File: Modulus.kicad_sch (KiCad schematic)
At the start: 208 parts, among them J1 USB_C_Receptacle_USB2.0_14P, SW1 Push_Button, U1 RP2040, U2 NCP1117-1.5_SOT223, U3 W25Q128JVS, Y1 12MHz

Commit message: added LEDs, may remove
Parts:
- added C100, C101, C102, C103, C104, C105, C106, C18, C19, C20, C21, C22, C23, C24, C25, C26, C27, C28, C29, C30, C31, C32, C33, C34, C35, C36, C37, C38, C39, C40, C41, C42, C43, C44, C45, C46, C47, C48, C49, C50, C51, C52, C53, C54, C55, C56, C57, C58, C59, C60, C61, C62, C63, C64, C65, C66, C67, C68, C69, C70, C71, C72, C73, C74, C75, C76, C77, C78, C79, C80, C81, C82, C83, C84, C85, C86, C87, C88, C89, C90, C91, C92, C93, C94, C95, C96, C97, C98, C99: 100nF, Capacitor_SMD:C_0402_1005Metric, symbol Device:C
- added D100, D101, D102, D103, D104, D105, D106, D107, D108, D109, D110, D111, D112, D113, D114, D115, D116, D117, D118, D119, D120, D121, D122, D123, D124, D125, D126, D127, D128, D129, D130, D131, D132, D133, D134, D135, D136, D137, D138, D139, D140, D141, D142, D143, D144, D145, D146, D147, D148, D149, D150, D151, D152, D153, D154, D155, D156, D157, D158, D159, D160, D161, D162, D163, D164, D165, D166, D167, D168, D169, D170, D171, D172, D173, D174, D175, D176, D177, D178, D179, D180, D181, D182, D183, D184, D90, D91, D92, D93, D94, D95, D96, D97, D98, D99: SK6812MINI, LED_SMD:LED_SK6812MINI_PLCC4_3.5x3.5mm_P1.75mm, symbol LED:SK6812MINI
- C15, C16: value 15pF -> 33pF
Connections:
- net +3V3: now also C100.2, C101.2, C102.2, C103.2, C104.2, C105.2, C106.2, C18.2, C19.2, C20.2, C21.2, C22.2, C23.2, C24.2, C25.2, C26.2, C27.2, C28.2, C29.2, C30.2, C31.2, C32.2, C33.2, C34.2, C35.2, C36.2, C37.2, C38.2, C39.2, C40.2, C41.2, C42.2, C43.2, C44.2, C45.2, C46.2, C47.2, C48.2, C49.2, C50.2, C51.2, C52.2, C53.2, C54.2, C55.2, C56.2, C57.2, C58.2, C59.2, C60.2, C61.2, C62.2, C63.2, C64.2, C65.2, C66.2, C67.2, C68.2, C69.2, C70.2, C71.2, C72.2, C73.2, C74.2, C75.2, C76.2, C77.2, C78.2, C79.2, C80.2, C81.2, C82.2, C83.2, C84.2, C85.2, C86.2, C87.2, C88.2, C89.2, C90.2, C91.2, C92.2, C93.2, C94.2, C95.2, C96.2, C97.2, C98.2, C99.2, D100.4 (VDD), D101.4 (VDD), D102.4 (VDD), D103.4 (VDD), D104.4 (VDD), D105.4 (VDD), D106.4 (VDD), D107.4 (VDD), D108.4 (VDD), D109.4 (VDD), D110.4 (VDD), D111.4 (VDD), D112.4 (VDD), D113.4 (VDD), D114.4 (VDD), D115.4 (VDD), D116.4 (VDD), D117.4 (VDD), D118.4 (VDD), D119.4 (VDD), D120.4 (VDD), D121.4 (VDD), D90.4 (VDD), D91.4 (VDD), D92.4 (VDD), D93.4 (VDD), D94.4 (VDD), D95.4 (VDD), D96.4 (VDD), D97.4 (VDD), D98.4 (VDD), D99.4 (VDD)
- net GND: now also C100.1, C101.1, C102.1, C103.1, C104.1, C105.1, C106.1, C18.1, C19.1, C20.1, C21.1, C22.1, C23.1, C24.1, C25.1, C26.1, C27.1, C28.1, C29.1, C30.1, C31.1, C32.1, C33.1, C34.1, C35.1, C36.1, C37.1, C38.1, C39.1, C40.1, C41.1, C42.1, C43.1, C44.1, C45.1, C46.1, C47.1, C48.1, C49.1, C50.1, C51.1, C52.1, C53.1, C54.1, C55.1, C56.1, C57.1, C58.1, C59.1, C60.1, C61.1, C62.1, C63.1, C64.1, C65.1, C66.1, C67.1, C68.1, C69.1, C70.1, C71.1, C72.1, C73.1, C74.1, C75.1, C76.1, C77.1, C78.1, C79.1, C80.1, C81.1, C82.1, C83.1, C84.1, C85.1, C86.1, C87.1, C88.1, C89.1, C90.1, C91.1, C92.1, C93.1, C94.1, C95.1, C96.1, C97.1, C98.1, C99.1, D100.2 (VSS), D101.2 (VSS), D102.2 (VSS), D103.2 (VSS), D104.2 (VSS), D105.2 (VSS), D106.2 (VSS), D107.2 (VSS), D108.2 (VSS), D109.2 (VSS), D110.2 (VSS), D111.2 (VSS), D112.2 (VSS), D113.2 (VSS), D114.2 (VSS), D115.2 (VSS), D116.2 (VSS), D117.2 (VSS), D118.2 (VSS), D119.2 (VSS), D120.2 (VSS), D121.2 (VSS), D137.2 (VSS), D138.2 (VSS), D139.2 (VSS), D140.2 (VSS), D141.2 (VSS), D142.2 (VSS), D143.2 (VSS), D144.2 (VSS), D145.2 (VSS), D146.2 (VSS), D147.2 (VSS), D148.2 (VSS), D149.2 (VSS), D150.2 (VSS), D151.2 (VSS), D152.2 (VSS), D153.2 (VSS), D154.2 (VSS), D155.2 (VSS), D156.2 (VSS), D157.2 (VSS), D158.2 (VSS), D159.2 (VSS), D160.2 (VSS), D161.2 (VSS), D162.2 (VSS), D163.2 (VSS), D164.2 (VSS), D165.2 (VSS), D166.2 (VSS), D167.2 (VSS), D168.2 (VSS), D169.2 (VSS), D170.2 (VSS), D171.2 (VSS), D172.2 (VSS), D173.2 (VSS), D174.2 (VSS), D175.2 (VSS), D176.2 (VSS), D177.2 (VSS), D178.2 (VSS), D179.2 (VSS), D180.2 (VSS), D181.2 (VSS), D182.2 (VSS), D183.2 (VSS), D184.2 (VSS), D90.2 (VSS), D91.2 (VSS), D92.2 (VSS), D93.2 (VSS), D94.2 (VSS), D95.2 (VSS), D96.2 (VSS), D97.2 (VSS), D98.2 (VSS), D99.2 (VSS)
- new net: D179.1 (DOUT), D180.3 (DIN)
- new net: D178.1 (DOUT), D179.3 (DIN)
- new net: D152.4 (VDD), D153.4 (VDD), D154.4 (VDD), D155.4 (VDD), D156.4 (VDD), D157.4 (VDD), D158.4 (VDD), D159.4 (VDD), D160.4 (VDD), D161.4 (VDD), D162.4 (VDD), D163.4 (VDD), D164.4 (VDD), D165.4 (VDD), D166.4 (VDD), D167.4 (VDD), D168.4 (VDD), D169.4 (VDD), D170.4 (VDD), D171.4 (VDD), D172.4 (VDD), D173.4 (VDD), D174.4 (VDD), D175.4 (VDD), D176.4 (VDD), D177.4 (VDD), D178.4 (VDD), D179.4 (VDD), D180.4 (VDD), D181.4 (VDD), D182.4 (VDD), D183.4 (VDD), D184.4 (VDD)
- new net: D144.1 (DOUT), D145.3 (DIN)
- new net: D143.1 (DOUT), D144.3 (DIN)
- new net: D122.4 (VDD), D123.4 (VDD), D124.4 (VDD), D125.4 (VDD), D126.4 (VDD), D127.4 (VDD), D128.4 (VDD), D129.4 (VDD), D130.4 (VDD), D131.4 (VDD), D132.4 (VDD), D133.4 (VDD), D134.4 (VDD), D135.4 (VDD), D136.4 (VDD), D137.4 (VDD), D138.4 (VDD), D139.4 (VDD), D140.4 (VDD), D141.4 (VDD), D142.4 (VDD), D143.4 (VDD), D144.4 (VDD), D145.4 (VDD), D146.4 (VDD), D147.4 (VDD), D148.4 (VDD), D149.4 (VDD), D150.4 (VDD), D151.4 (VDD)
- new net: D175.1 (DOUT), D176.3 (DIN)
- new net: D174.1 (DOUT), D175.3 (DIN)
- new net: D150.1 (DOUT), D151.3 (DIN)
- new net: D149.1 (DOUT), D150.3 (DIN)
- new net: D151.1 (DOUT), D152.3 (DIN)
- new net: D167.1 (DOUT), D168.3 (DIN)
- new net: D166.1 (DOUT), D167.3 (DIN)
- new net: D142.1 (DOUT), D143.3 (DIN)
- new net: D96.1 (DOUT), D97.3 (DIN)
- new net: D95.1 (DOUT), D96.3 (DIN)
- new net: D140.1 (DOUT), D141.3 (DIN)
- new net: D139.1 (DOUT), D140.3 (DIN)
- new net: D128.1 (DOUT), D129.3 (DIN)
- new net: D127.1 (DOUT), D128.3 (DIN)
- new net: D181.1 (DOUT), D182.3 (DIN)
- new net: D180.1 (DOUT), D181.3 (DIN)
- new net: D141.1 (DOUT), D142.3 (DIN)
- new net: D173.1 (DOUT), D174.3 (DIN)
- new net: D145.1 (DOUT), D146.3 (DIN)
- new net: D117.1 (DOUT), D118.3 (DIN)
- new net: D116.1 (DOUT), D117.3 (DIN)
- new net: D129.1 (DOUT), D130.3 (DIN)
- new net: D155.1 (DOUT), D156.3 (DIN)
- new net: D154.1 (DOUT), D155.3 (DIN)
- new net: D94.1 (DOUT), D95.3 (DIN)
- new net: D93.1 (DOUT), D94.3 (DIN)
- new net: D101.1 (DOUT), D102.3 (DIN)
- new net: D100.1 (DOUT), D101.3 (DIN)
- new net: D130.1 (DOUT), D131.3 (DIN)
- new net: D169.1 (DOUT), D170.3 (DIN)
- new net: D168.1 (DOUT), D169.3 (DIN)
- new net: D114.1 (DOUT), D115.3 (DIN)
- new net: D113.1 (DOUT), D114.3 (DIN)
- new net: D100.3 (DIN), D99.1 (DOUT)
- new net: D148.1 (DOUT), D149.3 (DIN)
- new net: D147.1 (DOUT), D148.3 (DIN)
- new net: D171.1 (DOUT), D172.3 (DIN)
- new net: D170.1 (DOUT), D171.3 (DIN)
- new net: D157.1 (DOUT), D158.3 (DIN)
- new net: D156.1 (DOUT), D157.3 (DIN)
- new net: D164.1 (DOUT), D165.3 (DIN)
- new net: D163.1 (DOUT), D164.3 (DIN)
- new net: D159.1 (DOUT), D160.3 (DIN)
- new net: D158.1 (DOUT), D159.3 (DIN)
- new net: D125.1 (DOUT), D126.3 (DIN)
- new net: D124.1 (DOUT), D125.3 (DIN)
- new net: D112.1 (DOUT), D113.3 (DIN)
- new net: D111.1 (DOUT), D112.3 (DIN)
- new net: D183.1 (DOUT), D184.3 (DIN)
- new net: D182.1 (DOUT), D183.3 (DIN)
- new net: D115.1 (DOUT), D116.3 (DIN)
- new net: D146.1 (DOUT), D147.3 (DIN)
- new net: D160.1 (DOUT), D161.3 (DIN)
- new net: D92.1 (DOUT), D93.3 (DIN)
- new net: D91.1 (DOUT), D92.3 (DIN)
- new net: D110.1 (DOUT), D111.3 (DIN)
- new net: D131.1 (DOUT), D132.3 (DIN)
- new net: D121.1 (DOUT), D122.3 (DIN)
- new net: D120.1 (DOUT), D121.3 (DIN)
- new net: D90.1 (DOUT), D91.3 (DIN)
- new net: D177.1 (DOUT), D178.3 (DIN)
- new net: D153.1 (DOUT), D154.3 (DIN)
- new net: D119.1 (DOUT), D120.3 (DIN)
- new net: D118.1 (DOUT), D119.3 (DIN)
- new net: D104.1 (DOUT), D105.3 (DIN)
- new net: D103.1 (DOUT), D104.3 (DIN)
- new net: D152.1 (DOUT), D153.3 (DIN)
- new net: D106.1 (DOUT), D107.3 (DIN)
- new net: D105.1 (DOUT), D106.3 (DIN)
- new net: D162.1 (DOUT), D163.3 (DIN)
- new net: D176.1 (DOUT), D177.3 (DIN)
- new net: D137.1 (DOUT), D138.3 (DIN)
- new net: D136.1 (DOUT), D137.3 (DIN)
- new net: D102.1 (DOUT), D103.3 (DIN)
- new net: D138.1 (DOUT), D139.3 (DIN)
- new net: D109.1 (DOUT), D110.3 (DIN)
- new net: D108.1 (DOUT), D109.3 (DIN)
- new net: D165.1 (DOUT), D166.3 (DIN)
- new net: D172.1 (DOUT), D173.3 (DIN)
- new net: D135.1 (DOUT), D136.3 (DIN)
- new net: D134.1 (DOUT), D135.3 (DIN)
- new net: D132.1 (DOUT), D133.3 (DIN)
- new net: D107.1 (DOUT), D108.3 (DIN)
- new net: D123.1 (DOUT), D124.3 (DIN)
- new net: D122.1 (DOUT), D123.3 (DIN)
- new net: D98.1 (DOUT), D99.3 (DIN)
- new net: D97.1 (DOUT), D98.3 (DIN)
- new net: D161.1 (DOUT), D162.3 (DIN)
- new net: D133.1 (DOUT), D134.3 (DIN)
- new net: D126.1 (DOUT), D127.3 (DIN)
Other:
- note added: "LED Matrix"
- note added: "Matrix Smoothing"
- company: (none) -> contykeys
- title: (none) -> Modules - Mainboard

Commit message: added a USB hub but don't really understand shit rn
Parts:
- removed C100, C101, C102, C103, C104, C105, C106, C18, C19, C20, C21, C22, C23, C24, C25, C26, C27, C28, C29, C30, C31, C32, C33, C34, C35, C36, C37, C38, C39, C40, C41, C42, C43, C44, C45, C46, C47, C48, C49, C50, C51, C52, C53, C54, C55, C56, C57, C58, C59, C60, C61, C62, C63, C64, C65, C66, C67, C68, C69, C70, C71, C72, C73, C74, C75, C76, C77, C78, C79, C80, C81, C82, C83, C84, C85, C86, C87, C88, C89, C90, C91, C92, C93, C94, C95, C96, C97, C98, C99: 100nF, Capacitor_SMD:C_0402_1005Metric, symbol Device:C
- removed D100, D101, D102, D103, D104, D105, D106, D107, D108, D109, D110, D111, D112, D113, D114, D115, D116, D117, D118, D119, D120, D121, D122, D123, D124, D125, D126, D127, D128, D129, D130, D131, D132, D133, D134, D135, D136, D137, D138, D139, D140, D141, D142, D143, D144, D145, D146, D147, D148, D149, D150, D151, D152, D153, D154, D155, D156, D157, D158, D159, D160, D161, D162, D163, D164, D165, D166, D167, D168, D169, D170, D171, D172, D173, D174, D175, D176, D177, D178, D179, D180, D181, D182, D183, D184, D90, D91, D92, D93, D94, D95, D96, D97, D98, D99: SK6812MINI, LED_SMD:LED_SK6812MINI_PLCC4_3.5x3.5mm_P1.75mm, symbol LED:SK6812MINI
- removed J1: USB_C_Receptacle_USB2.0_14P, symbol Connector:USB_C_Receptacle_USB2.0_14P
- removed R2: 5.1K, Resistor_THT:R_Axial_DIN0207_L6.3mm_D2.5mm_P10.16mm_Horizontal, symbol PCM_SL_Resistors:Resistor
- added GL850G1: GL850G, GL850G:28SSOP, symbol GL850G:GL850G
- added J2: USB_C_Receptacle_USB2.0_14P, symbol Connector:USB_C_Receptacle_USB2.0_14P
- added J3, J4: USB_A, symbol Connector:USB_A
- added R8, R9: 5.1K, Resistor_THT:R_Axial_DIN0207_L6.3mm_D2.5mm_P10.16mm_Horizontal, symbol PCM_SL_Resistors:Resistor
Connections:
- net +3V3: now also GL850G1.24 (3V3)
- net GND: now also GL850G1.15 (GND), J2.A1 (GND), J2.A12 (GND), J2.B1 (GND), J2.B12 (GND), J2.S1 (SHIELD), J3.4 (GND), J3.5 (Shield), J4.4 (GND), J4.5 (Shield), R8.2, R9.2
- net VBUS: now also GL850G1.23 (5V), J2.A4 (VBUS), J2.A9 (VBUS), J2.B4 (VBUS), J2.B9 (VBUS), J3.1 (VBUS), J4.1 (VBUS)
- net at R1.1: now also GL850G1.4 (RREF)
- new net: J2.A5 (CC1), R8.1
- new net: J2.B5 (CC2), R9.1
- new net HOST_USB_D+: GL850G1.26 (DP0), J2.A6 (D+), J2.B6 (D+)
- new net HOST_USB_D-: GL850G1.25 (DM0), J2.A7 (D-), J2.B7 (D-)
- new net PORT1_USB_D+: GL850G1.28 (DP1), J3.3 (D+)
- new net PORT1_USB_D-: GL850G1.27 (DM1), J3.2 (D-)
- new net PORT2_USB_D+: GL850G1.3 (DP2), J4.3 (D+)
- new net PORT2_USB_D-: GL850G1.2 (DM2), J4.2 (D-)
- new net RP2040_USB_D+: GL850G1.9 (DP3)
- new net RP2040_USB_D-: GL850G1.8 (DM3)
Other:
- note removed: "LED Matrix"
- note removed: "Matrix Smoothing"
- moved on the sheet: C1, C10, C11, C12, C13, C14, C15, C16, C2, C3, C4, C5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

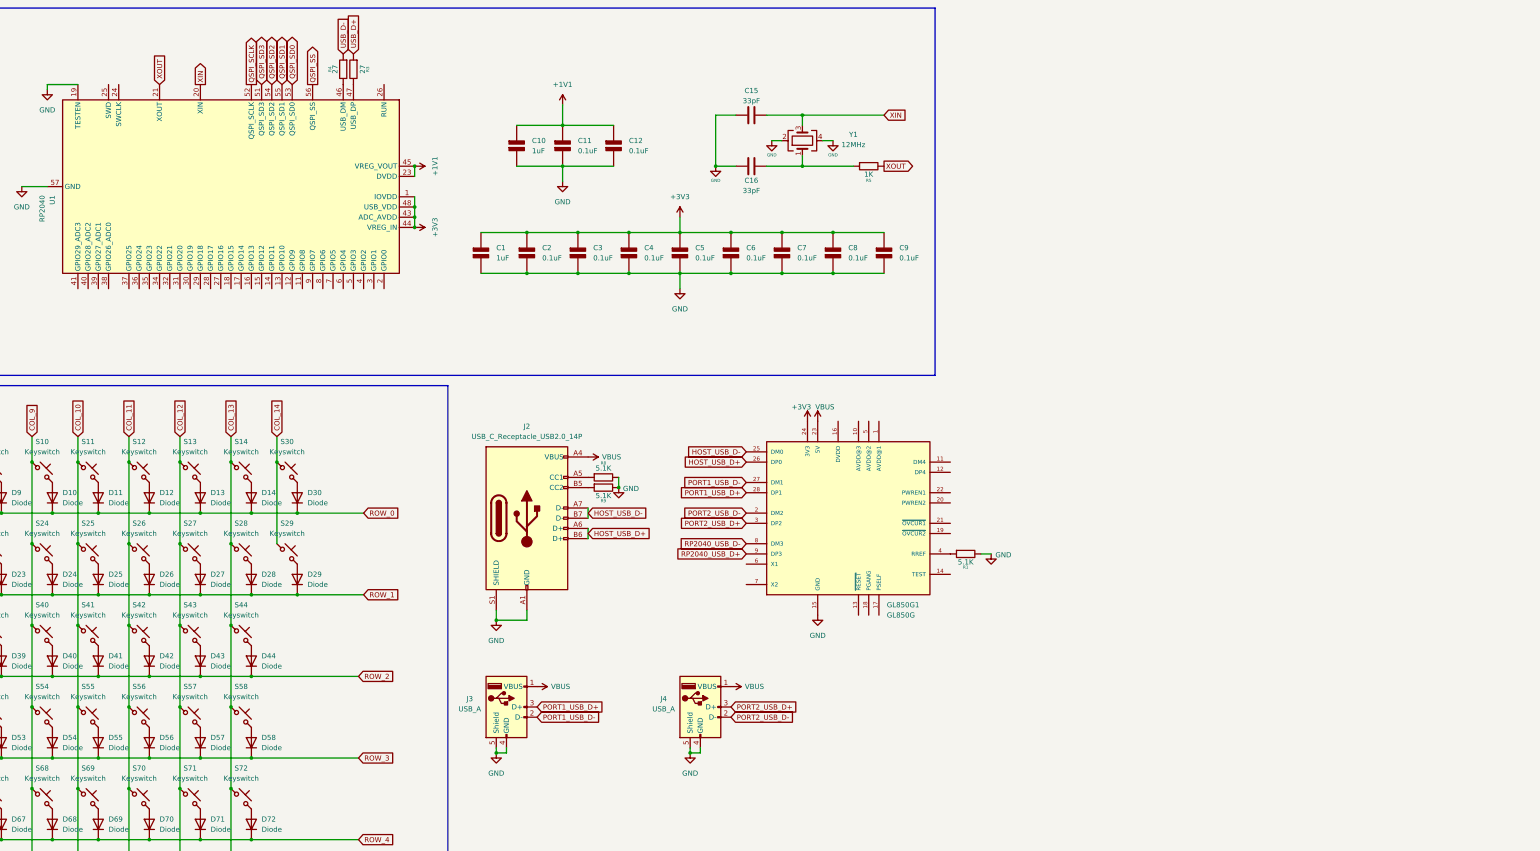
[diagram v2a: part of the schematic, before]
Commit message: added my own OLED screen, XLR ports, and a caps lock LEd
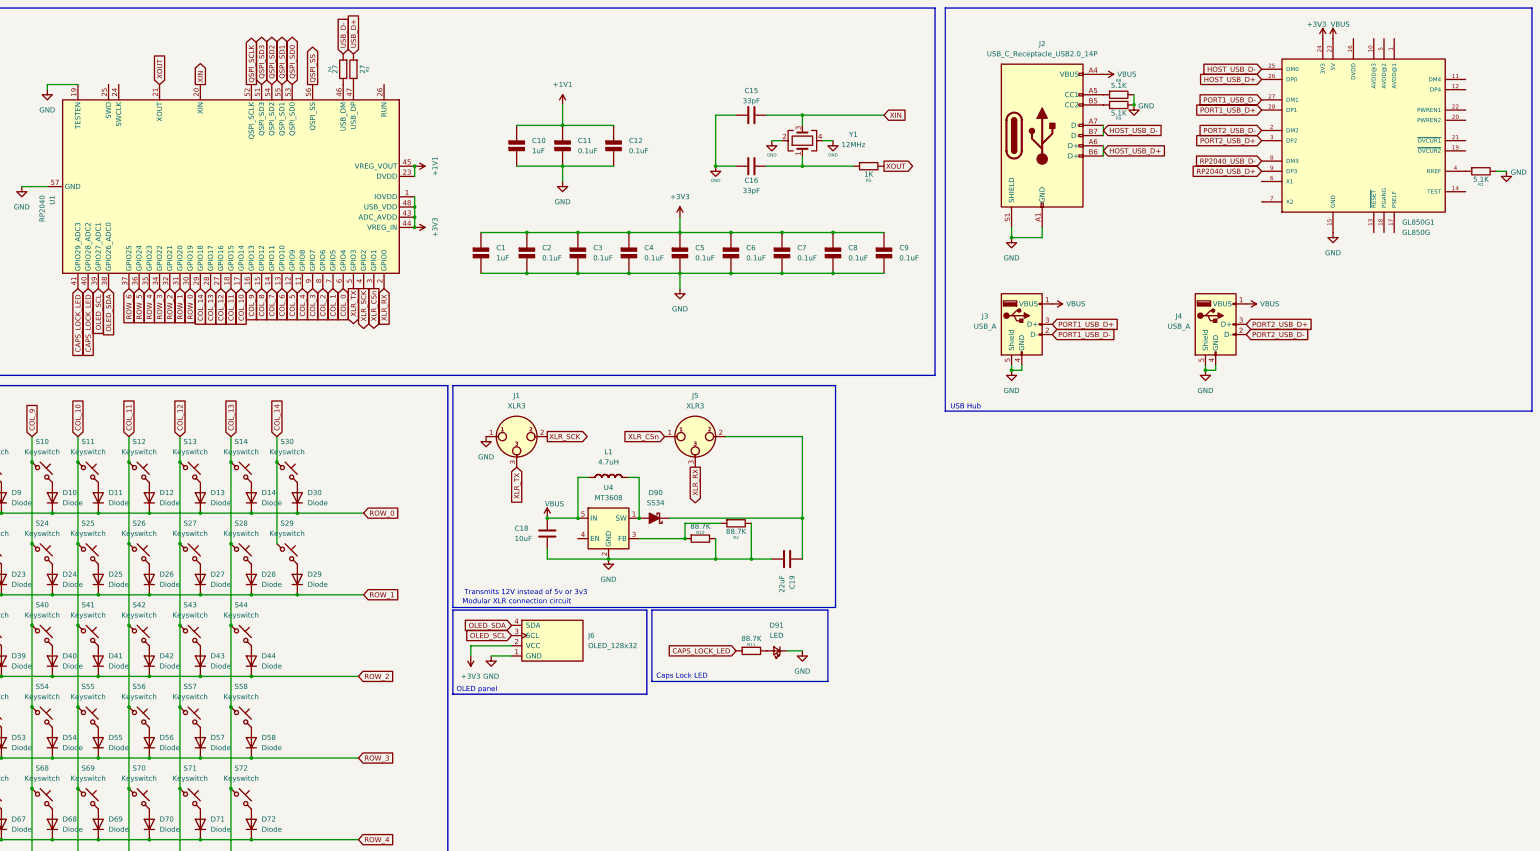
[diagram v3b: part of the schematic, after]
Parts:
- added C18: 10uF, symbol Device:C
- added C19: 22uF, symbol Device:C
- added D90: SS34, PCM_Diode_SMD_AKL:D_SMC, symbol PCM_Diode_Schottky_AKL:SS34
- added D91: LED, SparkFun-LED:LED_0603_1608Metric, symbol SparkFun-LED:LED
- added J1, J5: XLR3, symbol Connector_Audio:XLR3
- added J6: OLED_128x32, ScottoKeebs_Components:OLED_128x32, symbol SCOTOKEEBS:OLED_128x32
- added L1: 4.7uH, symbol PCM_Elektuur:L
- added R10, R11, R2: 88.7K, Resistor_THT:R_Axial_DIN0207_L6.3mm_D2.5mm_P10.16mm_Horizontal, symbol PCM_SL_Resistors:Resistor
- added U4: MT3608, Package_TO_SOT_SMD:SOT-23-6, symbol Regulator_Switching:MT3608
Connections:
- net +3V3: now also J6.2 (VCC)
- net COL_0: now also U1.6 (GPIO4)
- net COL_1: now also U1.7 (GPIO5)
- net COL_10: now also U1.17 (GPIO14)
- net COL_11: now also U1.18 (GPIO15)
- net COL_12: now also U1.27 (GPIO16)
- net COL_13: now also U1.28 (GPIO17)
- net COL_14: now also U1.29 (GPIO18)
- net COL_2: now also U1.8 (GPIO6)
- net COL_3: now also U1.9 (GPIO7)
- net COL_4: now also U1.11 (GPIO8)
- net COL_5: now also U1.12 (GPIO9)
- net COL_6: now also U1.13 (GPIO10)
- net COL_7: now also U1.14 (GPIO11)
- net COL_8: now also U1.15 (GPIO12)
- net COL_9: now also U1.16 (GPIO13)
- net GND: now also C18.2, C19.2, D91.1 (K), J1.1, J6.1 (GND), R10.2, R2.2, U4.2 (GND)
- net ROW_0: now also U1.30 (GPIO19)
- net ROW_1: now also U1.31 (GPIO20)
- net ROW_2: now also U1.32 (GPIO21)
- net ROW_3: now also U1.34 (GPIO22)
- net ROW_4: now also U1.35 (GPIO23)
- net ROW_5: now also U1.36 (GPIO24)
- net ROW_6: now also U1.37 (GPIO25)
- net VBUS: now also C18.1, L1.1 (+), U4.5 (IN)
- net XLR_RX: now reaches U1.2 (GPIO0)
- net XLR_RX: now also J5.3
- net XLR_CSn: now reaches U1.3 (GPIO1)
- net XLR_CSn: now also J5.1
- net OLED_SDA: now reaches U1.38 (GPIO26_ADC0)
- net OLED_SDA: now also J6.4 (SDA)
- net OLED_SCL: now reaches U1.39 (GPIO27_ADC1)
- net OLED_SCL: now also J6.3 (SCL)
- net XLR_SCK: now reaches U1.4 (GPIO2)
- net XLR_SCK: now also J1.2
- net CAPS_LOCK_LED: now reaches U1.40 (GPIO28_ADC2)
- net CAPS_LOCK_LED: now also U1.41 (GPIO29_ADC3), R11.1
- net XLR_TX: now reaches U1.5 (GPIO3)
- net XLR_TX: now also J1.3
- new net: D90.2 (A), L1.2 (-), U4.1 (SW)
- new net: R10.1, R2.1, U4.3 (FB)
- new net: D91.2 (A), R11.2
- new net: C19.1, D90.1 (K), J5.2
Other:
- note added: "Caps Lock LED"
- note added: "Modular XLR connection circuit"
- note added: "OLED panel"
- note added: "Transmits 12V instead of 5v or 3v3"
- note added: "USB Hub"
- moved on the sheet: GL850G1, J2, J3, J4, R1, R8, R9
